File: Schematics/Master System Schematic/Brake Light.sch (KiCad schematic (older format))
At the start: 3 parts, among them U10 KY-019, U13 CAN_Bus_Module

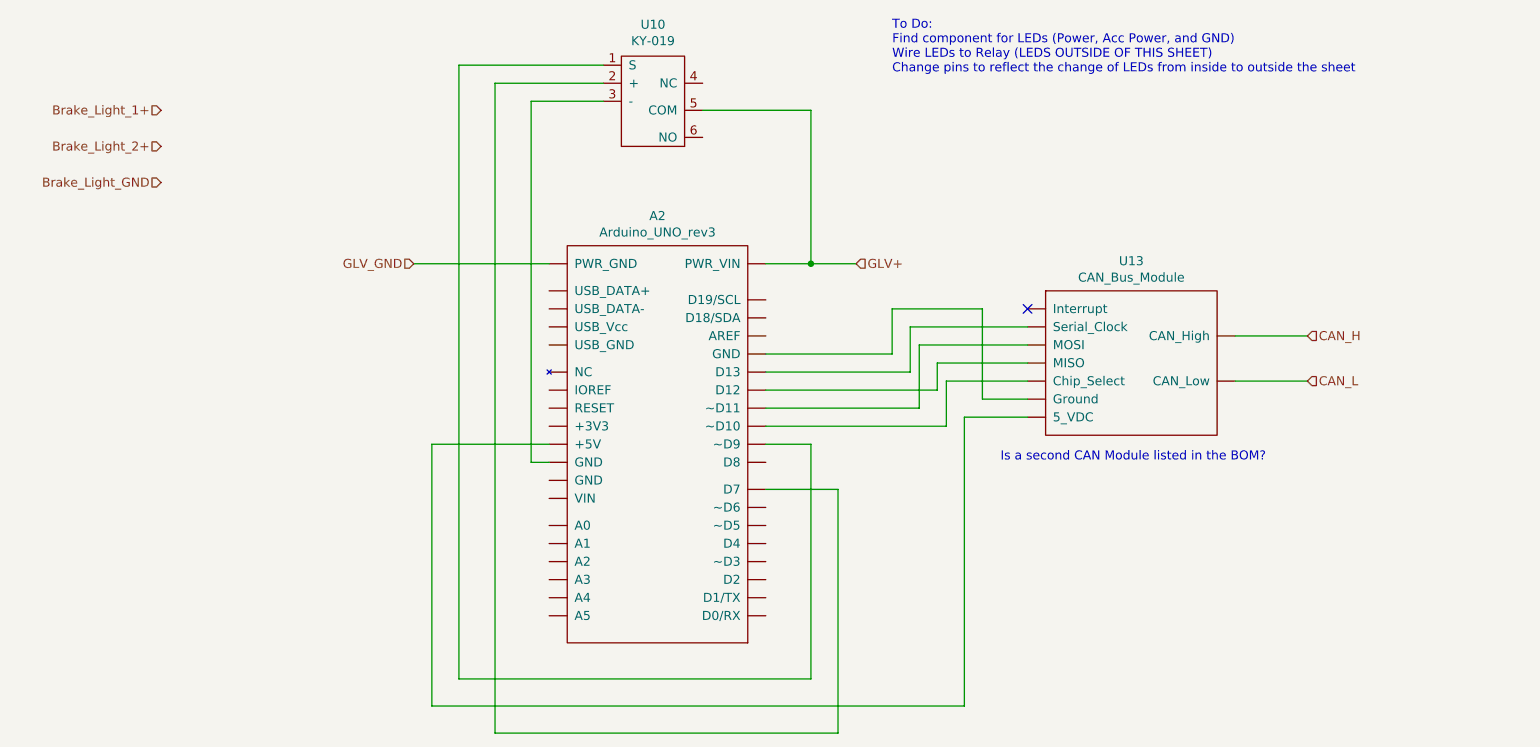
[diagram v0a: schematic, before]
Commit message: Added Brake LED Symbol and Finished Brake Light Sheet
Final Julius draft of Brake Light and IO sheets before I get Cam to check if my connections are all true.
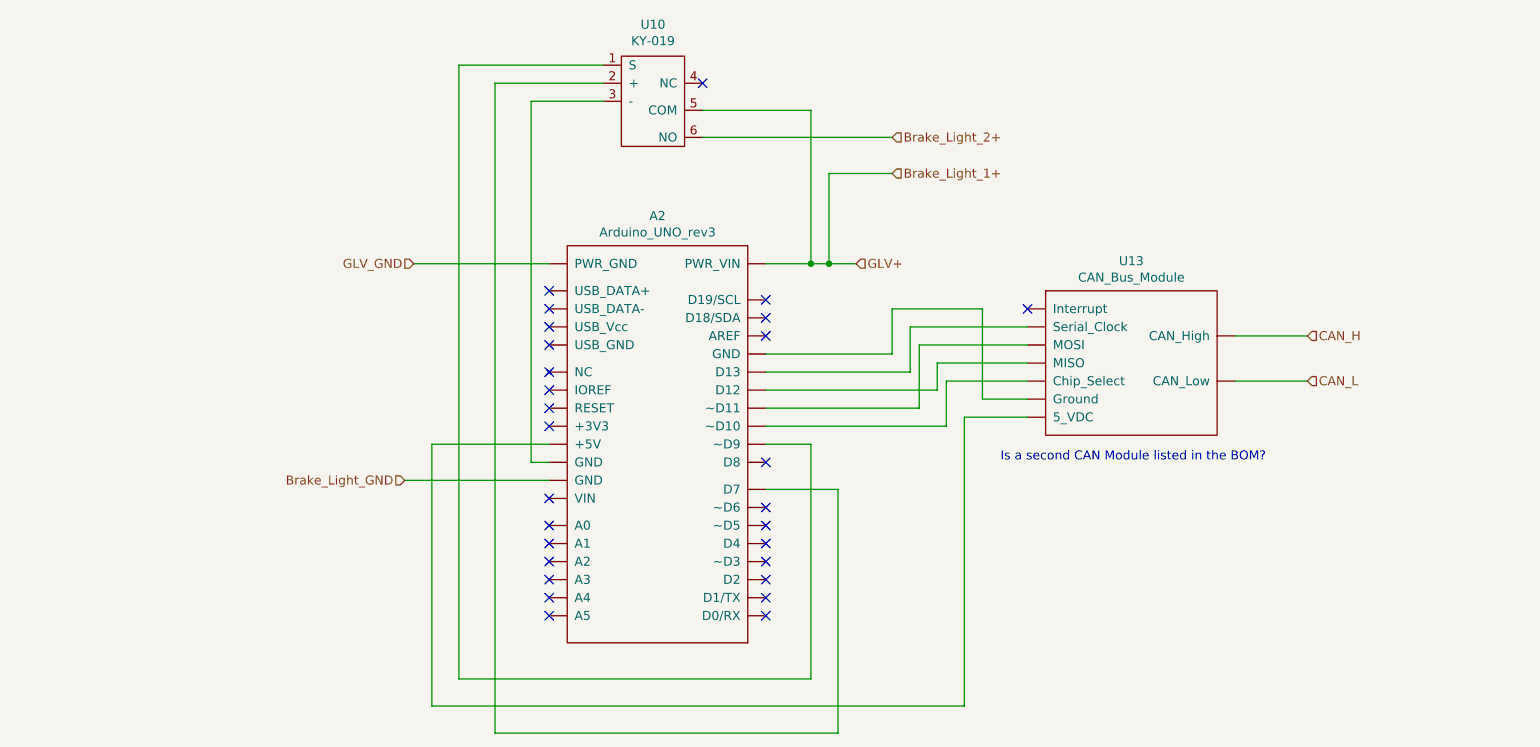
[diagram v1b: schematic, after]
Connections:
- net Brake_Light_1+: now also A2.~ (~~D9), U10.5 (COM)
- net Brake_Light_2+: now also U10.6 (NO)
- net Brake_Light_GND: now also A2.~ (~~D9)
- removed net GLV+: A2.~ (~~D9), U10.5 (COM)
- new net: A2.~ (~~D9), U13.~ (Serial_Clock) (x6)
- no-connect marks 1 -> 28
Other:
- note removed: "To Do:\nFind component for LEDs (Power, Acc Power, and GND)\nWire LEDs to Relay (LEDS OUTSIDE OF THIS SHEET)\nChange pins to reflect the change of LEDs from inside to outside the sheet"
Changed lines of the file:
@@
 Text HLabel 5800 2850 2    50   Input ~ 0
 GLV+
-Wire Wire Line
-	5800 2850 5550 2850
 Text HLabel 3350 2850 0    50   Input ~ 0
 GLV_GND
@@
 Wire Wire Line
 	5550 3850 5300 3850
-Text HLabel 1950 2000 0    50   Input ~ 0
+Text HLabel 6000 2350 2    50   Input ~ 0
 Brake_Light_1+
-Text HLabel 1950 2200 0    50   Input ~ 0
+Text HLabel 6000 2150 2    50   Input ~ 0
 Brake_Light_2+
-Text HLabel 1950 2400 0    50   Input ~ 0
+Text HLabel 3300 4050 0    50   Input ~ 0
 Brake_Light_GND
 Wire Wire Line
@@
 Wire Wire Line
 	4000 3950 4100 3950
-Text Notes 6000 1800 0    50   ~ 0
-To Do:\nFind component for LEDs (Power, Acc Power, and GND)\nWire LEDs to Relay (LEDS OUTSIDE OF THIS SHEET)\nChange pins to reflect the change of LEDs from inside to outside the sheet
+Wire Wire Line
+	5550 2850 5650 2850
+Wire Wire Line
+	4950 2150 6000 2150
+Wire Wire Line
+	6000 2350 5650 2350
+Wire Wire Line
+	5650 2350 5650 2850
+Connection ~ 5650 2850
+Wire Wire Line
+	5650 2850 5800 2850
+Wire Wire Line
+	4100 4050 3300 4050
+NoConn ~ 4950 1850
+NoConn ~ 5300 3050
+NoConn ~ 5300 3150
+NoConn ~ 5300 3250
+NoConn ~ 5300 3950
+NoConn ~ 5300 4200
+NoConn ~ 5300 4300
+NoConn ~ 5300 4400
+NoConn ~ 5300 4500
+NoConn ~ 5300 4600
+NoConn ~ 5300 4700
+NoConn ~ 5300 4800
+NoConn ~ 4100 4800
+NoConn ~ 4100 4700
+NoConn ~ 4100 4600
+NoConn ~ 4100 4500
+NoConn ~ 4100 4400
+NoConn ~ 4100 4300
+NoConn ~ 4100 4150
+NoConn ~ 4100 3750
+NoConn ~ 4100 3650
+NoConn ~ 4100 3550
+NoConn ~ 4100 3450
+NoConn ~ 4100 3300
+NoConn ~ 4100 3200
+NoConn ~ 4100 3100
+NoConn ~ 4100 3000
 $EndSCHEMATC

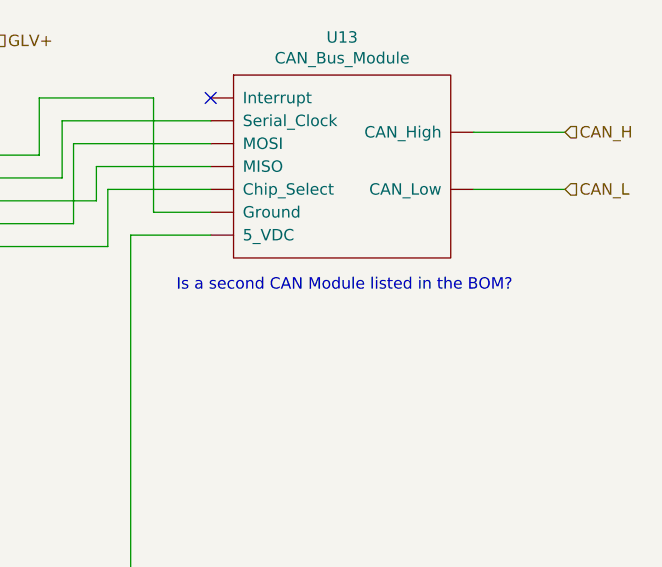
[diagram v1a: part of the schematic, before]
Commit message: Removed Text Notes, Changed LED(+) Label (Was LED(-))
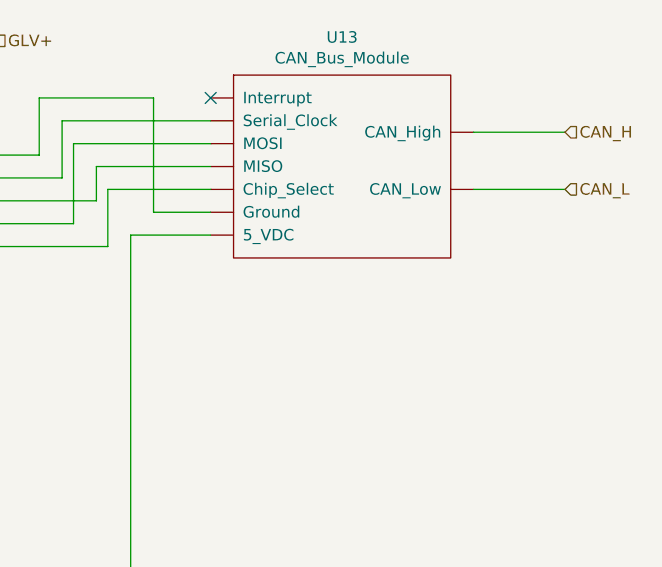
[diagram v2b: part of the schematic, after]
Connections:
- new net: A2.~ (~~D9), U13.~ (Serial_Clock) (x6)
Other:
- note removed: "Is a second CAN Module listed in the BOM?"
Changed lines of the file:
@@
 	1    0    0    -1
 $EndComp
-Text Notes 6600 3950 0    50   ~ 0
-Is a second CAN Module listed in the BOM?
 NoConn ~ 6750 3100
 Wire Wire Line

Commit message: Fixed Master
Readded all the things lost in the merge on master.
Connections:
- new net: A2.~ (~~D9), U13.~ (Serial_Clock) (x6)
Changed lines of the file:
@@
 Sheet 13 13
 Title ""
-Date ""
+Date "2020-10-12"
 Rev ""
 Comp ""
